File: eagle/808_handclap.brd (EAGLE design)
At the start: 100 x 80.3 mm, 94 parts, among them IC1 LM339N, IC2 TL072P, IC3 TL072P, Q28 BC546, Q29 BC556, Q35 BC546, Q69 BC546, Q70 BC546, Q71 BC556, Q72 BC556, Q73 BC546, U1 POWER, U22 BA6110SIL

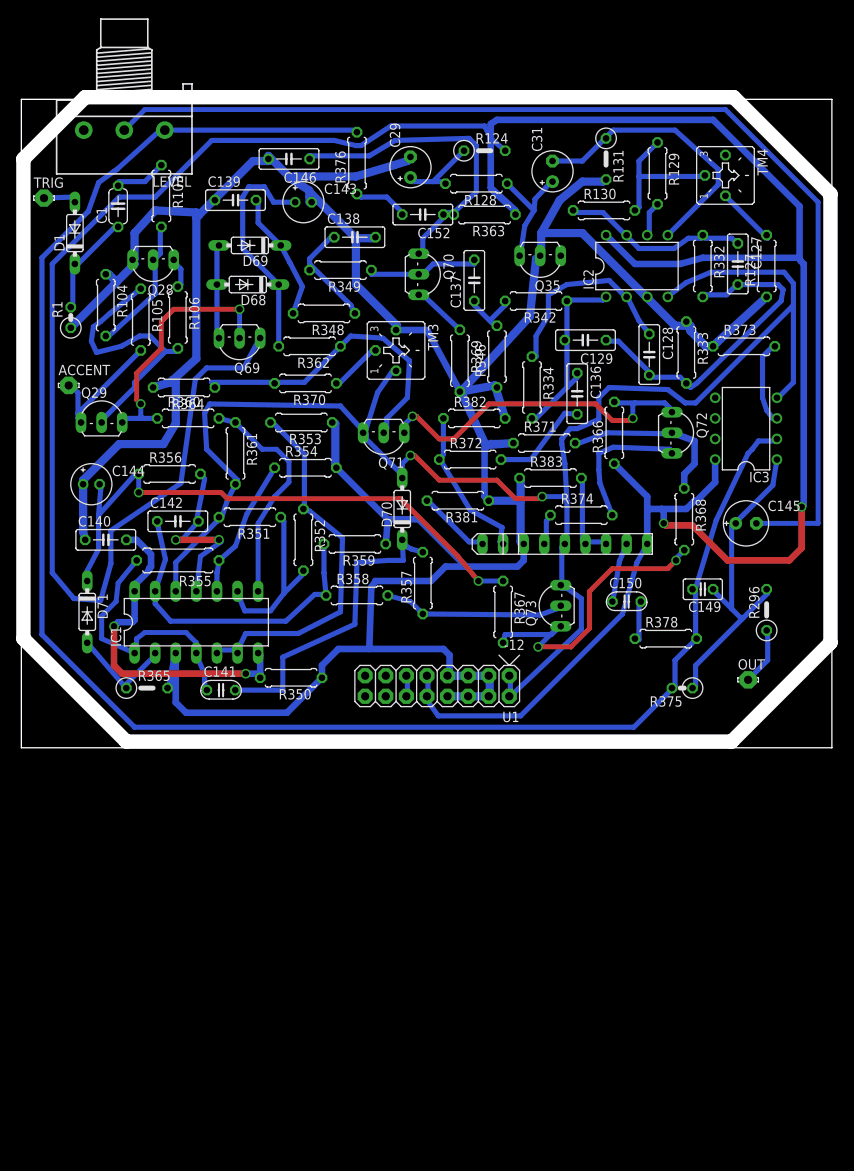
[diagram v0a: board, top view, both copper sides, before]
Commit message: 2n3904 and 2n3906
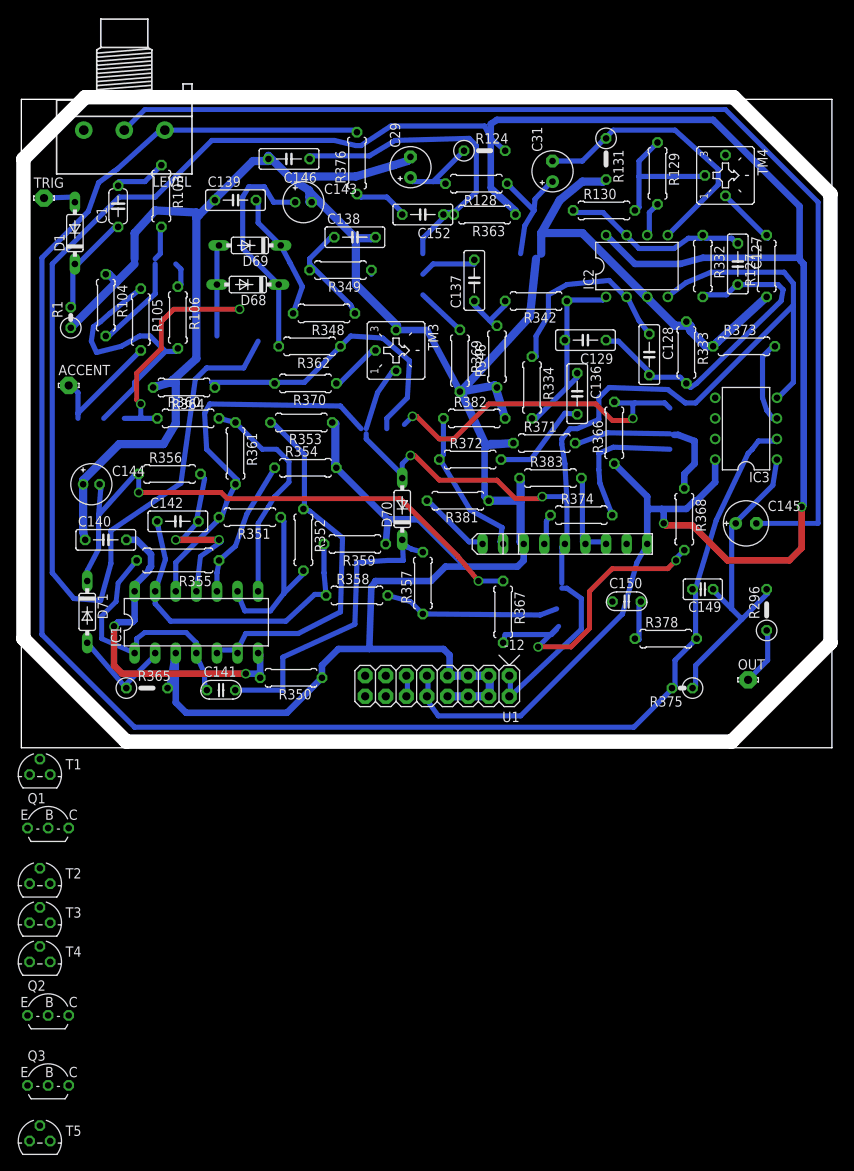
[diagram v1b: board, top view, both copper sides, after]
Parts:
- removed Q28, Q35, Q69, Q70, Q73: BC546, transistor:TO92-CBE
- removed Q29, Q71, Q72: BC556, transistor:TO92-EBC
- added Q1, Q2, Q3: 2N3906INLINE, mes_transistors:TO92-CBE
- added T1, T2, T3, T4, T5: 2N3904, transistor:TO92
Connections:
- removed net N$63: C150.P$1, U22.8
- net +12V: now also T3.1; no longer Q69.C
- net -12V: now also Q2.C, T5.3; no longer Q71.C, Q73.E
- net CPTRIG: now also Q1.C, T3.2; no longer Q29.C, Q69.B
- net GND: now also T1.3, T4.2; no longer Q28.E, Q35.B
- net N$37: now also Q1.B; no longer Q29.B
- net N$38: now also T1.1; no longer Q28.C
- net N$4: now also T1.2; no longer Q28.B
- net N$40: now also T2.2; no longer Q70.B
- net N$42: now also T2.3; no longer Q70.E
- net N$44: now also T3.3; no longer Q69.E
- net N$46: now also T2.1; no longer Q70.C
- net N$48: now also Q2.B; no longer Q71.B
- net N$61: now also C150.P$1; no longer U22.7
- net N$66: now also Q3.B; no longer Q72.B
- net N$67: now also Q2.E, Q3.E; no longer Q71.E, Q72.E
- net N$69: now also Q3.C; no longer Q72.C
- net N$695: now also T4.3; no longer Q35.E
- net N$70: now also T5.1; no longer Q73.C
- net N$75: now also T5.2; no longer Q73.B
- net TRIG: now also Q1.E; no longer Q29.E
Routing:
- net N$63: track 7.36 -> 0.00 mm
- net N$40: track 14.2 -> 7.89 mm
- net CPTRIG: track 32.0 -> 27.9 mm
- net -12V: track 199.9 -> 197.6 mm
- net TRIG: track 17.4 -> 15.6 mm
- net GND: track 390.5 -> 388.7 mm
- net N$67: track 43.2 -> 41.7 mm
- net N$70: track 37.9 -> 37.1 mm
- net N$4: track 16.9 -> 16.0 mm
- net N$66: track 21.6 -> 21.0 mm
- net N$75: track 22.3 -> 21.7 mm
- net N$48: track 38.7 -> 38.0 mm
- net N$38: track 3.83 -> 3.26 mm
- net N$37: track 34.3 -> 33.7 mm
- net N$69: track 17.4 -> 16.8 mm
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
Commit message: gcode for converted version
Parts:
- R124, R296: device TR808clone:0207/5V -> TR808clone:0207/7
- R375: device TR808clone:0207/2V -> TR808clone:0207/7
- T1, T2, T3, T4, T5: value 2N3904 -> 2N3904INLINE; device transistor:TO92 -> bt_transistor:TO92-CBE
- moved Q3 111.4 mm to (80.3, 38.9), turned to 270 degrees
- moved T4 106.6 mm to (63.8, 60.7)
- moved T5 91.8 mm to (66.3, 17.3), turned to 270 degrees
- moved T2 88.9 mm to (49.3, 58.7), turned to 90 degrees
- moved Q2 83.5 mm to (45.0, 39.4), turned to 180 degrees
- moved T3 76.6 mm to (26.7, 51.1)
- moved T1 64.6 mm to (16.5, 59.7)
- moved Q1 51.0 mm to (9.91, 40.6)
- moved LEVEL 2.05 mm to (14.7, 76.5)
- moved C152 1.37 mm to (48.3, 66.3)
- moved R124 0.92 mm to (56.6, 72.9)
- moved R372 0.80 mm to (56.1, 35.3)
- moved R381 0.76 mm to (54.6, 30.5)
- moved C29 0.57 mm to (47.8, 71.1), turned to 180 degrees
- moved C128 0.36 mm to (77.2, 48.8)
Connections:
- net +12V: now also T3.C; no longer T3.1
- net -12V: now also T5.E; no longer T5.3
- net CPTRIG: now also T3.B; no longer T3.2
- net GND: now also T1.E, T4.B; no longer T1.3, T4.2
- net N$38: now also T1.C; no longer T1.1
- net N$4: now also T1.B; no longer T1.2
- net N$40: now also T2.B; no longer T2.2
- net N$42: now also T2.E; no longer T2.3
- net N$44: now also T3.E; no longer T3.3
- net N$46: now also T2.C; no longer T2.1
- net N$695: now also T4.E; no longer T4.3
- net N$70: now also T5.C; no longer T5.1
- net N$75: now also T5.B; no longer T5.2
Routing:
- net N$61: track 10.6 -> 16.9 mm
- net N$40: track 7.89 -> 14.0 mm
- net CPTRIG: track 27.9 -> 31.0 mm
- net N$696: track 10.1 -> 7.59 mm
- net GND: track 388.7 -> 386.3 mm
- net N$46: track 39.0 -> 41.2 mm
- net +12V: track 374.8 -> 376.8 mm
- net N$57: track 6.76 -> 4.95 mm
- net N$92: track 213.6 -> 212.0 mm
- net N$95: track 138.6 -> 137.4 mm
- net N$55: track 12.3 -> 11.5 mm
- net N$56: track 19.4 -> 20.1 mm
- net N$67: track 41.7 -> 42.3 mm
- net N$59: track 9.04 -> 9.55 mm
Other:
- board size 100 x 80.3 mm -> 100 x 80.8 mm
